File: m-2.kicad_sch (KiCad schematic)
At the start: 0 parts

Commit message: Add layout for expansion connector and M.2 key M slot
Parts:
- added A1: Bus_M.2_1-2199230-6, antmicro-footprints:Bus_M.2_Socket_Key_M_TE_1-2199230-6, symbol antmicroPciConnectors:Bus_M.2_1-2199230-6
- added C6, C7: C_10u_0402, antmicro-footprints:C_0402_1005Metric, symbol antmicroCapacitors0402:C_10u_0402
- added C8: C_100n_0603, antmicro-footprints:C_0603_1608Metric, symbol antmicroCapacitors0603:C_100n_0603
- added D1: LED_G_0603_KP-1608ZGC, antmicro-footprints:LED_0603_1608Metric_G, symbol antmicroLEDIndicationDiscrete:LED_G_0603_KP-1608ZGC
- added R3: R_4k7_0402, antmicro-footprints:R_0402_1005Metric, symbol antmicroResistors0402:R_4k7_0402
- added R4, R5, R6: R_0R_0603, antmicro-footprints:R_0603_1608Metric, symbol antmicroResistors0603:R_0R_0603
- added R7: R_200R_0402, antmicro-footprints:R_0402_1005Metric, symbol antmicroResistors0402:R_200R_0402
- added TP4, TP5, TP6: TP_1.5mm_SMD, antmicro-footprints:TP_SMD_1.5mm, symbol antmicroTestPoints:TP_1.5mm_SMD
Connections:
- new net: R3.1, R6.1
- new net: D1.1, R7.1
- new net: A1.10 (LED), D1.2
- new net +3V3: A1.12 (3V3), A1.14 (3V3), A1.16 (3V3), A1.18 (3V3), A1.2 (3V3), A1.4 (3V3), A1.70 (3V3), A1.72 (3V3), A1.74 (3V3), C6.2, C7.2, C8.2, R3.2, R7.2
- new net GND: A1.1 (GND), A1.15 (GND), A1.21 (GND), A1.27 (GND), A1.3 (GND), A1.33 (GND), A1.39 (GND), A1.45 (GND), A1.51 (GND), A1.57 (GND), A1.71 (GND), A1.73 (GND), A1.75 (GND), A1.9 (GND), A1.SH (SHIELD), C6.1, C7.1, C8.1
- new net M2_M_SMB_CLK: A1.40 (SMB_CLK), TP6.1
- new net M2_M_SMB_DATA: A1.42 (SMB_DATA), TP5.1
- new net M2_M_SUSCLK: A1.68 (SUSCLK)
- new net PCIE2_CLKREQ: R5.1
- new net PCIE2_CLK_N: A1.53 (REFCLK_N)
- new net PCIE2_CLK_P: A1.55 (REFCLK_P)
- new net PCIE2_RST: R4.1
- new net PCIE2_RX0_N: A1.41 (PER0_N)
- new net PCIE2_RX0_P: A1.43 (PER0_P)
- new net PCIE2_RX1_N: A1.29 (PER1_N)
- new net PCIE2_RX1_P: A1.31 (PER1_P)
- new net PCIE2_TX0_N: A1.47 (PET0_N)
- new net PCIE2_TX0_P: A1.49 (PET0_P)
- new net PCIE2_TX1_N: A1.35 (PET1_N)
- new net PCIE2_TX1_P: A1.37 (PET1_P)
- new net ~{M2_M_ALERT}: A1.44 (ALERT), TP4.1
- new net ~{M2_M_CLKREQ0}: A1.52 (~{CLKREQ}), R5.2
- new net ~{M2_M_PERST}: A1.50 (~{PERST}), R4.2
- new net ~{M2_M_PEWAKE0}: A1.54 (~{PEWAKE}), R6.2
- no-connect marks 0 -> 8
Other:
- note added: "3V3_M2"
- note added: "NOTE: Place bulk caps near to the M.2 power pads"

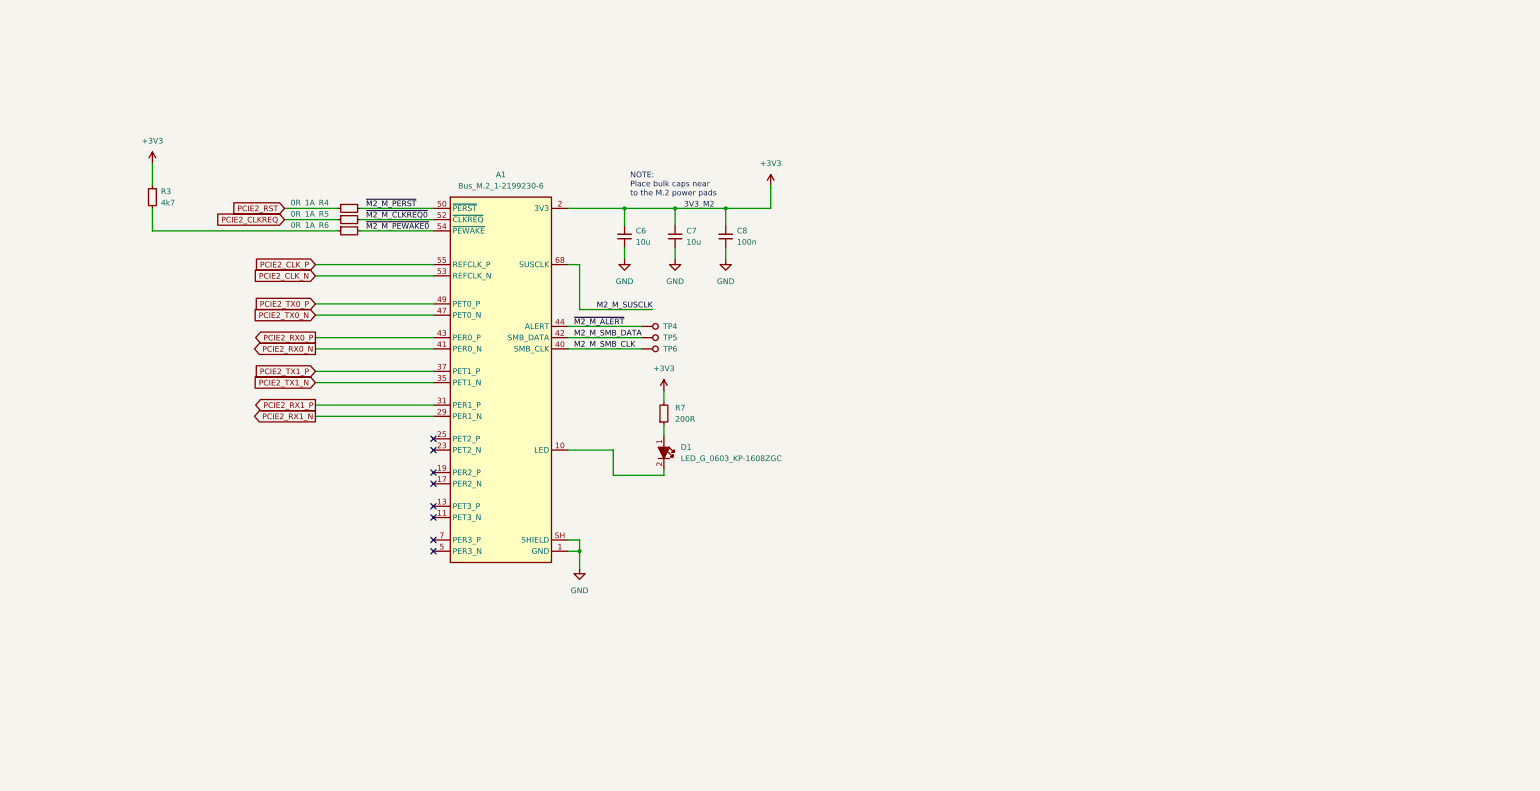
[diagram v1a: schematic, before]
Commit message: [#45539] Finish schematic + draw dif pairs and other signals
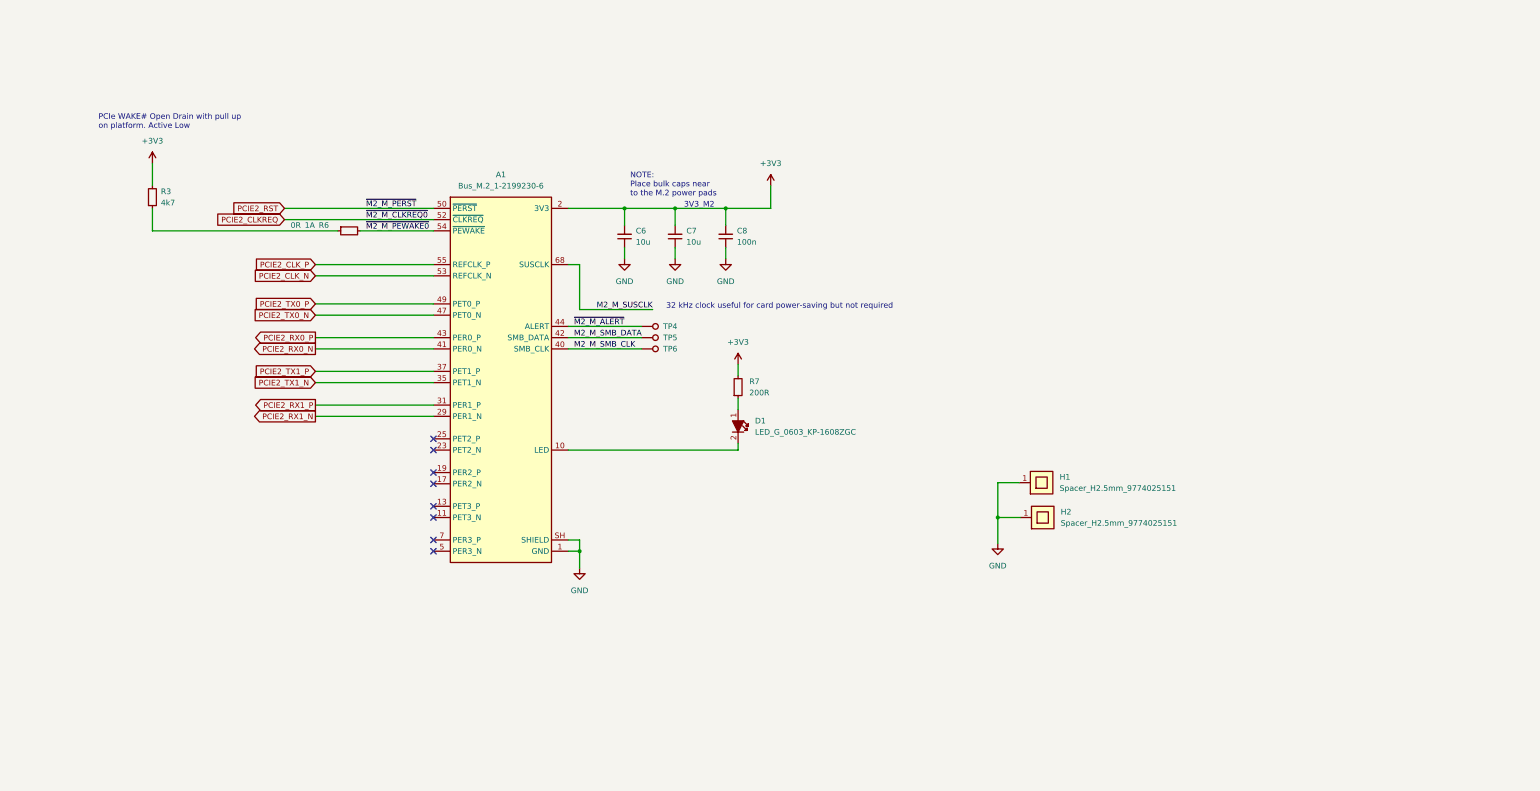
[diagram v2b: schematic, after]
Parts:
- removed R4, R5: R_0R_0603, antmicro-footprints:R_0603_1608Metric, symbol antmicroResistors0603:R_0R_0603
- added H1, H2: Spacer_H2.5mm_9774025151, antmicro-footprints:Spacer_SMD_M2.5_H2.5mm_Wurth_9774025151, symbol antmicroMechanicalParts:Spacer_H2.5mm_9774025151
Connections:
- net ~{M2_M_CLKREQ0} is gone; now on net PCIE2_CLKREQ: A1.52 (~{CLKREQ})
- net ~{M2_M_PERST} is gone; now on net PCIE2_RST: A1.50 (~{PERST})
- net GND: now also H1.1, H2.1
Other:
- note added: "32 kHz clock useful for card power-saving but not required"
- note added: "PCIe WAKE# Open Drain with pull up on platform. Active Low"
- moved on the sheet: D1, R7

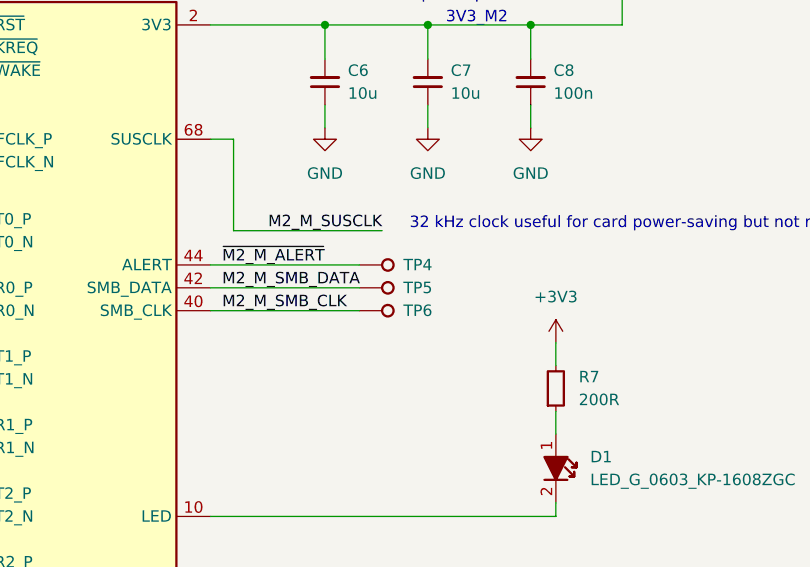
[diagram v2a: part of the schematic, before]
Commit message: [#45539] Change spacing of the m2 spacers, fix DRC, prepare labels for sd card reader
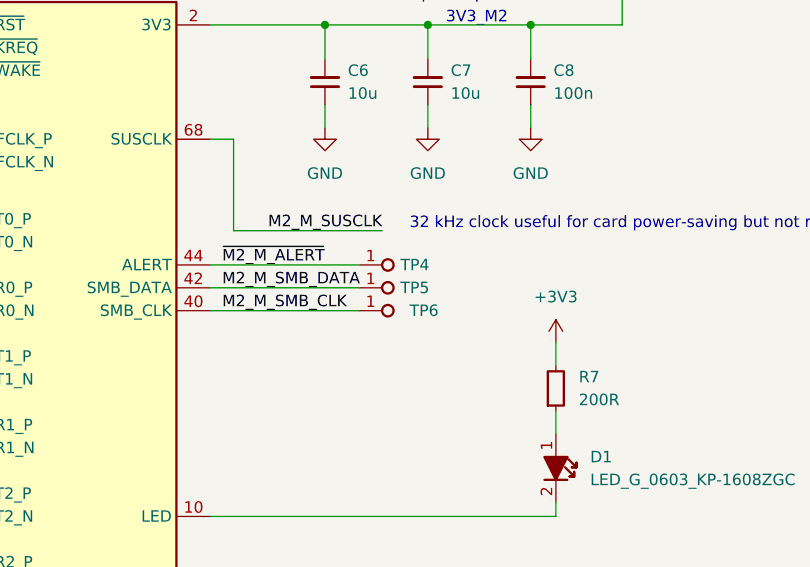
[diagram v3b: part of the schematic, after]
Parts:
- removed TP4, TP5, TP6: TP_1.5mm_SMD, antmicro-footprints:TP_SMD_1.5mm, symbol antmicroTestPoints:TP_1.5mm_SMD
- added TP4, TP5, TP6: TP_0.75mm_SMD, antmicro-footprints:TP_SMD_0.75mm, symbol antmicroTestPoints:TP_0.75mm_SMD
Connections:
- net M2_M_SMB_CLK: now also TP6.1
- net M2_M_SMB_DATA: now also TP5.1
- net ~{M2_M_ALERT}: now also TP4.1
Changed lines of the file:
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@@
-    (pin "1")
-  )
-  (symbol (lib_id "antmicroTestPoints:TP_1.5mm_SMD") (at 147.32 86.36 0) (unit 1)
-    (in_bom yes) (on_board yes)
-    (property "Reference" "TP5" (id 0) (at 155.448 86.36 0)
-      (effects (font (size 1.27 1.27) (thickness 0.15)) (justify right))
-    )
-    (property "Value" "TP_1.5mm_SMD" (id 1) (at 152.4 78.994 90)
-      (effects (font (size 1.27 1.27) (thickness 0.15)) (justify right) hide)
-    )
-    (property "Footprint" "antmicro-footprints:TP_SMD_1.5mm" (id 2) (at 162.56 96.52 0)
-      (effects (font (size 1.27 1.27) (thickness 0.15)) (justify left bottom) hide)
-    )
-    (property "Datasheet" "" (id 3) (at 162.56 99.06 0)
-      (effects (font (size 1.27 1.27) (thickness 0.15)) (justify left bottom) hide)
-    )
-    (property "MPN" "" (id 4) (at 147.32 86.36 0)
-      (effects (font (size 1.27 1.27)) hide)
-    )
-    (property "Manufacturer" "" (id 5) (at 147.32 86.36 0)
-      (effects (font (size 1.27 1.27)) hide)
-    )
-    (property "Author" "Antmicro" (id 6) (at 162.56 101.6 0)
-      (effects (font (size 1.27 1.27) (thickness 0.15)) (justify left bottom) hide)
-    )
-    (property "License" "Apache-2.0" (id 7) (at 162.56 104.14 0)
-      (effects (font (size 1.27 1.27) (thickness 0.15)) (justify left bottom) hide)
-    )
     (pin "1")
   )
@@
     (pin "1")
   )
+  (symbol (lib_id "antmicroTestPoints:TP_0.75mm_SMD") (at 147.32 88.9 0) (unit 1)
+    (in_bom yes) (on_board yes) (fields_autoplaced)
+    (property "Reference" "TP6" (id 0) (at 152.908 88.8999 0)
+      (effects (font (size 1.27 1.27) (thickness 0.15)) (justify left))
+    )
+    (property "Value" "TP_0.75mm_SMD" (id 1) (at 162.56 96.52 0)
+      (effects (font (size 1.27 1.27) (thickness 0.15)) (justify left bottom) hide)
+    )
+    (property "Footprint" "antmicro-footprints:TP_SMD_0.75mm" (id 2) (at 162.56 99.06 0)
+      (effects (font (size 1.27 1.27) (thickness 0.15)) (justify left bottom) hide)
+    )
+    (property "Datasheet" "" (id 3) (at 162.56 101.6 0)
+      (effects (font (size 1.27 1.27) (thickness 0.15)) (justify left bottom) hide)
+    )
+    (property "MPN" "" (id 4) (at 147.32 88.9 0)
+      (effects (font (size 1.27 1.27)) hide)
+    )
+    (property "Manufacturer" "" (id 5) (at 147.32 88.9 0)
+      (effects (font (size 1.27 1.27)) hide)
+    )
+    (property "Author" "Antmicro" (id 6) (at 162.56 104.14 0)
+      (effects (font (size 1.27 1.27) (thickness 0.15)) (justify left bottom) hide)
+    )
+    (property "License" "Apache-2.0" (id 7) (at 162.56 106.68 0)
+      (effects (font (size 1.27 1.27) (thickness 0.15)) (justify left bottom) hide)
+    )
+    (pin "1")
+  )
   (symbol (lib_id "antmicroLEDIndicationDiscrete:LED_G_0603_KP-1608ZGC") (at 169.164 102.616 270) (unit 1)
     (in_bom yes) (on_board yes) (fields_autoplaced)
@@
     (pin "1")
     (pin "2")
+  )
+  (symbol (lib_id "antmicroTestPoints:TP_0.75mm_SMD") (at 147.32 86.36 0) (unit 1)
+    (in_bom yes) (on_board yes) (fields_autoplaced)
+    (property "Reference" "TP5" (id 0) (at 151.892 86.3599 0)
+      (effects (font (size 1.27 1.27) (thickness 0.15)) (justify left))
+    )
+    (property "Value" "TP_0.75mm_SMD" (id 1) (at 162.56 93.98 0)
+      (effects (font (size 1.27 1.27) (thickness 0.15)) (justify left bottom) hide)
+    )
+    (property "Footprint" "antmicro-footprints:TP_SMD_0.75mm" (id 2) (at 162.56 96.52 0)
+      (effects (font (size 1.27 1.27) (thickness 0.15)) (justify left bottom) hide)
+    )
+    (property "Datasheet" "" (id 3) (at 162.56 99.06 0)
+      (effects (font (size 1.27 1.27) (thickness 0.15)) (justify left bottom) hide)
+    )
+    (property "MPN" "" (id 4) (at 147.32 86.36 0)
+      (effects (font (size 1.27 1.27)) hide)
+    )
+    (property "Manufacturer" "" (id 5) (at 147.32 86.36 0)
+      (effects (font (size 1.27 1.27)) hide)
+    )
+    (property "Author" "Antmicro" (id 6) (at 162.56 101.6 0)
+      (effects (font (size 1.27 1.27) (thickness 0.15)) (justify left bottom) hide)
+    )
+    (property "License" "Apache-2.0" (id 7) (at 162.56 104.14 0)
+      (effects (font (size 1.27 1.27) (thickness 0.15)) (justify left bottom) hide)
+    )
+    (pin "1")
   )
   (symbol (lib_id "antmicropower:+3V3") (at 169.164 92.456 0) (unit 1)
@@
     (pin "1")
   )
+  (symbol (lib_id "antmicroTestPoints:TP_0.75mm_SMD") (at 147.32 83.82 0) (unit 1)
+    (in_bom yes) (on_board yes) (fields_autoplaced)
+    (property "Reference" "TP4" (id 0) (at 151.892 83.8199 0)
+      (effects (font (size 1.27 1.27) (thickness 0.15)) (justify left))
+    )
+    (property "Value" "TP_0.75mm_SMD" (id 1) (at 162.56 91.44 0)
+      (effects (font (size 1.27 1.27) (thickness 0.15)) (justify left bottom) hide)
+    )
+    (property "Footprint" "antmicro-footprints:TP_SMD_0.75mm" (id 2) (at 162.56 93.98 0)
+      (effects (font (size 1.27 1.27) (thickness 0.15)) (justify left bottom) hide)
+    )
+    (property "Datasheet" "" (id 3) (at 162.56 96.52 0)
+      (effects (font (size 1.27 1.27) (thickness 0.15)) (justify left bottom) hide)
+    )
+    (property "MPN" "" (id 4) (at 147.32 83.82 0)
+      (effects (font (size 1.27 1.27)) hide)
+    )
+    (property "Manufacturer" "" (id 5) (at 147.32 83.82 0)
+      (effects (font (size 1.27 1.27)) hide)
+    )
+    (property "Author" "Antmicro" (id 6) (at 162.56 99.06 0)
+      (effects (font (size 1.27 1.27) (thickness 0.15)) (justify left bottom) hide)
+    )
+    (property "License" "Apache-2.0" (id 7) (at 162.56 101.6 0)
+      (effects (font (size 1.27 1.27) (thickness 0.15)) (justify left bottom) hide)
+    )
+    (pin "1")
+  )
   (symbol (lib_id "antmicroResistors0402:R_4k7_0402") (at 36.83 57.15 90) (unit 1)
     (in_bom yes) (on_board yes) (fields_autoplaced)
@@
     (pin "1")
     (pin "2")
-  )
-  (symbol (lib_id "antmicroTestPoints:TP_1.5mm_SMD") (at 147.32 83.82 0) (unit 1)
-    (in_bom yes) (on_board yes)
-    (property "Reference" "TP4" (id 0) (at 155.448 83.82 0)
-      (effects (font (size 1.27 1.27) (thickness 0.15)) (justify right))
-    )
-    (property "Value" "TP_1.5mm_SMD" (id 1) (at 152.4 76.454 90)
-      (effects (font (size 1.27 1.27) (thickness 0.15)) (justify right) hide)
-    )
-    (property "Footprint" "antmicro-footprints:TP_SMD_1.5mm" (id 2) (at 162.56 93.98 0)
-      (effects (font (size 1.27 1.27) (thickness 0.15)) (justify left bottom) hide)
-    )
-    (property "Datasheet" "" (id 3) (at 162.56 96.52 0)
-      (effects (font (size 1.27 1.27) (thickness 0.15)) (justify left bottom) hide)
-    )
-    (property "MPN" "" (id 4) (at 147.32 83.82 0)
-      (effects (font (size 1.27 1.27)) hide)
-    )
-    (property "Manufacturer" "" (id 5) (at 147.32 83.82 0)
-      (effects (font (size 1.27 1.27)) hide)
-    )
-    (property "Author" "Antmicro" (id 6) (at 162.56 99.06 0)
-      (effects (font (size 1.27 1.27) (thickness 0.15)) (justify left bottom) hide)
-    )
-    (property "License" "Apache-2.0" (id 7) (at 162.56 101.6 0)
-      (effects (font (size 1.27 1.27) (thickness 0.15)) (justify left bottom) hide)
-    )
-    (pin "1")
   )
   (symbol (lib_id "antmicroMechanicalParts:Spacer_H2.5mm_9774025151") (at 232.918 127 0) (unit 1)
@@
     (pin "2")
   )
-  (symbol (lib_id "antmicroTestPoints:TP_1.5mm_SMD") (at 147.32 88.9 0) (unit 1)
-    (in_bom yes) (on_board yes)
-    (property "Reference" "TP6" (id 0) (at 155.448 88.9 0)
-      (effects (font (size 1.27 1.27) (thickness 0.15)) (justify right))
-    )
-    (property "Value" "TP_1.5mm_SMD" (id 1) (at 152.4 81.534 90)
-      (effects (font (size 1.27 1.27) (thickness 0.15)) (justify right) hide)
-    )
-    (property "Footprint" "antmicro-footprints:TP_SMD_1.5mm" (id 2) (at 162.56 99.06 0)
-      (effects (font (size 1.27 1.27) (thickness 0.15)) (justify left bottom) hide)
-    )
-    (property "Datasheet" "" (id 3) (at 162.56 101.6 0)
-      (effects (font (size 1.27 1.27) (thickness 0.15)) (justify left bottom) hide)
-    )
-    (property "MPN" "" (id 4) (at 147.32 88.9 0)
-      (effects (font (size 1.27 1.27)) hide)
-    )
-    (property "Manufacturer" "" (id 5) (at 147.32 88.9 0)
-      (effects (font (size 1.27 1.27)) hide)
-    )
-    (property "Author" "Antmicro" (id 6) (at 162.56 104.14 0)
-      (effects (font (size 1.27 1.27) (thickness 0.15)) (justify left bottom) hide)
-    )
-    (property "License" "Apache-2.0" (id 7) (at 162.56 106.68 0)
-      (effects (font (size 1.27 1.27) (thickness 0.15)) (justify left bottom) hide)
-    )
-    (pin "1")
-  )
   (symbol (lib_id "antmicropower:+3V3") (at 36.83 46.99 0) (unit 1)

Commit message: [#45539] Apply changes after review
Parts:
- removed R6: R_0R_0603, antmicro-footprints:R_0603_1608Metric, symbol antmicroResistors0603:R_0R_0603
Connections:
- net ~{M2_M_PEWAKE0}: now also R3.1
- no-connect marks 8 -> 9
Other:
- note added: "M.2 connector"
- moved on the sheet: A1, C6, C7, C8, D1, H1, H2, R3, R7, TP4, TP5, TP6
